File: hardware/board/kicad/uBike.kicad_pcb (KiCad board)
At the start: 2 copper layers, 60 x 80 mm, 56 parts, among them J1 KMDGX-6S-BS, J2 F31S-1A7L1-11040, J3 KMDGX-8S-BS, J4 TC2050-IDC-NL, J5 87520-0010BLF, Q1 MMBT3904, U1 SN65HVD08DR, U2 LD1117S33TR_SOT223, U3 MDBT50Q-P1MV2, U4 PTPSM863252RDXR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

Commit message: Schematic cleanup
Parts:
- C1, C10, C3, C7: value 100nF -> 100n
- C11: value 22pF -> 22p
- C12: value 33uF -> 33u
- C2, C4, C8: value 10uF -> 10u
- C5, C6: value 12pF -> 12p
- C9: value 10nF -> 10n
- moved R15 5.79 mm to (78.0, 46.0), turned to 0 degrees
- moved R14 4.32 mm to (78.0, 40.4), turned to 0 degrees
- moved D1 1.82 mm to (75.5, 43.2), turned to 180 degrees
- moved R13 0.06 mm to (78.8, 43.2)
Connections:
- D1 pad 1: RS485_A -> RS485_B
- D1 pad 2: RS485_B -> RS485_A
- J3 pad 3: Net-(J3-Pad3) -> RS485_B
- J3 pad 4: Net-(J3-Pad4) -> RS485_A
- R13 pad 1: RS485_B -> Net-(U1-B)
- R13 pad 2: RS485_A -> Net-(U1-A)
- R14 pad 1: RS485_B -> RS485_A
- R14 pad 2: Net-(J3-Pad3) -> Net-(U1-A)
- R15 pad 1: RS485_A -> RS485_B
- R15 pad 2: Net-(J3-Pad4) -> Net-(U1-B)
- U1 pad 6: RS485_A -> Net-(U1-A)
- U1 pad 7: RS485_B -> Net-(U1-B)
- U3 pad 3: IN4 -> unconnected-(U3-P1.10-Pad3)
- U3 pad 5: unconnected-(U3-P1.12-Pad5) -> IN4
- U4 pad 10: unconnected-(U4-SW-Pad2) -> (no net)
- U4 pad 11: unconnected-(U4-SW-Pad2) -> (no net)
- U4 pad 12: unconnected-(U4-SW-Pad2) -> (no net)
- U4 pad 13: unconnected-(U4-SW-Pad2) -> (no net)
- U4 pad 14: +5V -> (no net)
- U4 pad 15: +5V -> (no net)
- U4 pad 16: +5V -> (no net)
- U4 pad 17: +5V -> (no net)
- U4 pad 18: +5V -> (no net)
- U4 pad 19: +5V -> (no net)
- U4 pad 8: unconnected-(U4-SW-Pad2) -> (no net)
- U4 pad 9: unconnected-(U4-SW-Pad2) -> (no net)
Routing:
- net Net-(U1-A): track 0.00 -> 23.7 mm
- net Net-(U1-B): track 0.00 -> 23.3 mm
- net RS485_A: track 26.0 -> 10.5 mm, vias 2 -> 1
- net Net-(J3-Pad3): track 14.7 -> 0.00 mm, vias 1 -> 0
- net Net-(J3-Pad4): track 8.51 -> 0.00 mm, vias 1 -> 0
- net RS485_B: track 28.3 -> 22.0 mm, vias 4 -> 1
- net GND: track 0.00 -> 2.77 mm, vias 61 -> 55
- net IN1: track 44.3 -> 42.5 mm
- net IN4: track 37.8 -> 39.4 mm
- net IN3: track 43.0 -> 42.3 mm
- net IN2: track 48.4 -> 47.7 mm

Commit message: Finalized for review
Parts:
- moved R20 8.20 mm to (100.1, 84.5)
- moved D2 6.71 mm to (100.1, 82.0), turned to 0 degrees
- moved J4 4.84 mm to (105.9, 88.0), turned to 90 degrees
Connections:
- U3 pad 36: unconnected-(U3-P0.14-Pad36) -> YU
- U3 pad 57: YU -> unconnected-(U3-P1.06-Pad57)
- U4 pad 10: (no net) -> unconnected-(U4-SW-Pad2)
- U4 pad 11: (no net) -> unconnected-(U4-SW-Pad2)
- U4 pad 12: (no net) -> unconnected-(U4-SW-Pad2)
- U4 pad 13: (no net) -> unconnected-(U4-SW-Pad2)
- U4 pad 14: (no net) -> +5V
- U4 pad 15: (no net) -> +5V
- U4 pad 16: (no net) -> +5V
- U4 pad 17: (no net) -> +5V
- U4 pad 18: (no net) -> +5V
- U4 pad 19: (no net) -> +5V
- U4 pad 8: (no net) -> unconnected-(U4-SW-Pad2)
- U4 pad 9: (no net) -> unconnected-(U4-SW-Pad2)
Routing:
- net GND: track 2.77 -> 26.7 mm, vias 55 -> 69
- net +3.3V: track 132.7 -> 144.2 mm
- net Net-(D2-A): track 17.4 -> 7.79 mm, vias 2 -> 0
- net SWD_RST: track 10.4 -> 19.0 mm
- net SWO: track 10.5 -> 17.6 mm
- net YU: track 46.1 -> 42.0 mm
- net BL_PWM: track 22.2 -> 24.5 mm
- net SWCLK: track 13.9 -> 11.9 mm, vias 2 -> 0
- net CTP_SDA: track 42.7 -> 43.4 mm
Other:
- board text removed: "Greco Engineering Solutions LLC"

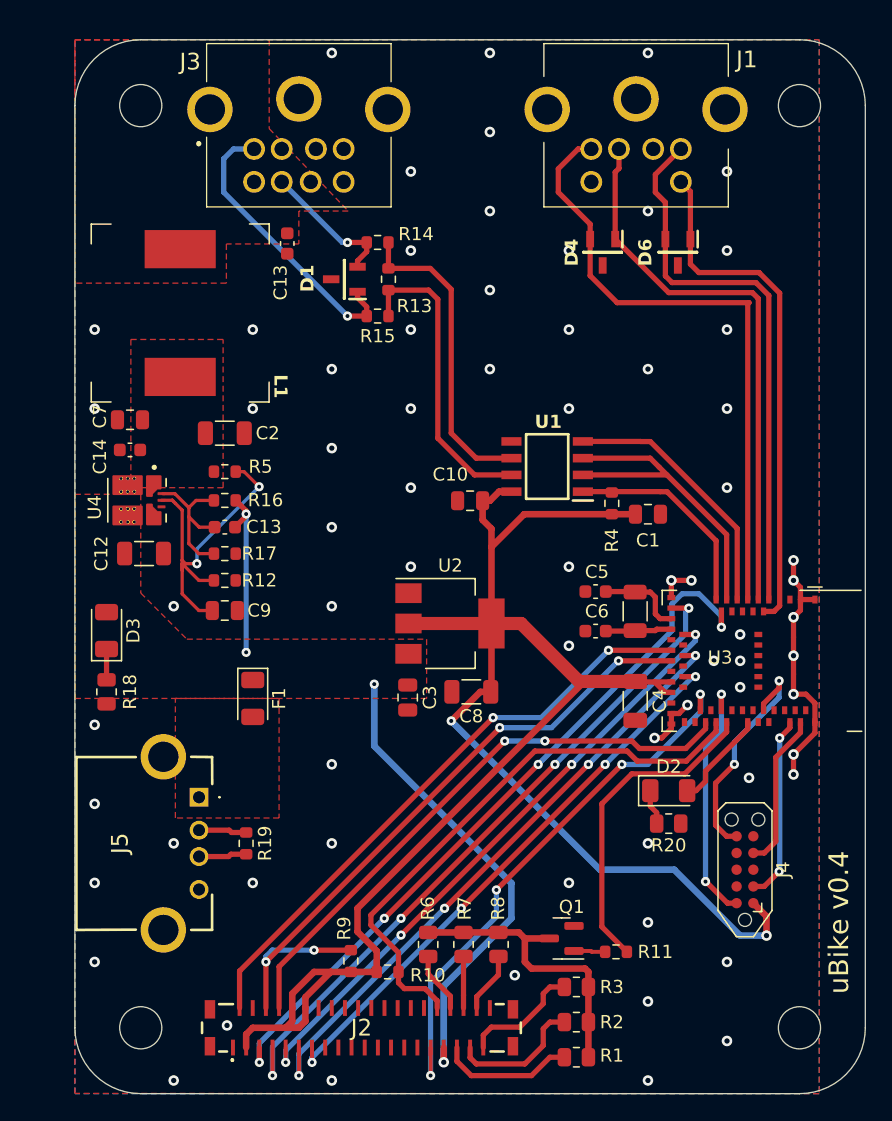
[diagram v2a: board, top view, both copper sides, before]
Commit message: Changed 2.2uF cap footprints and a bit more cleanup
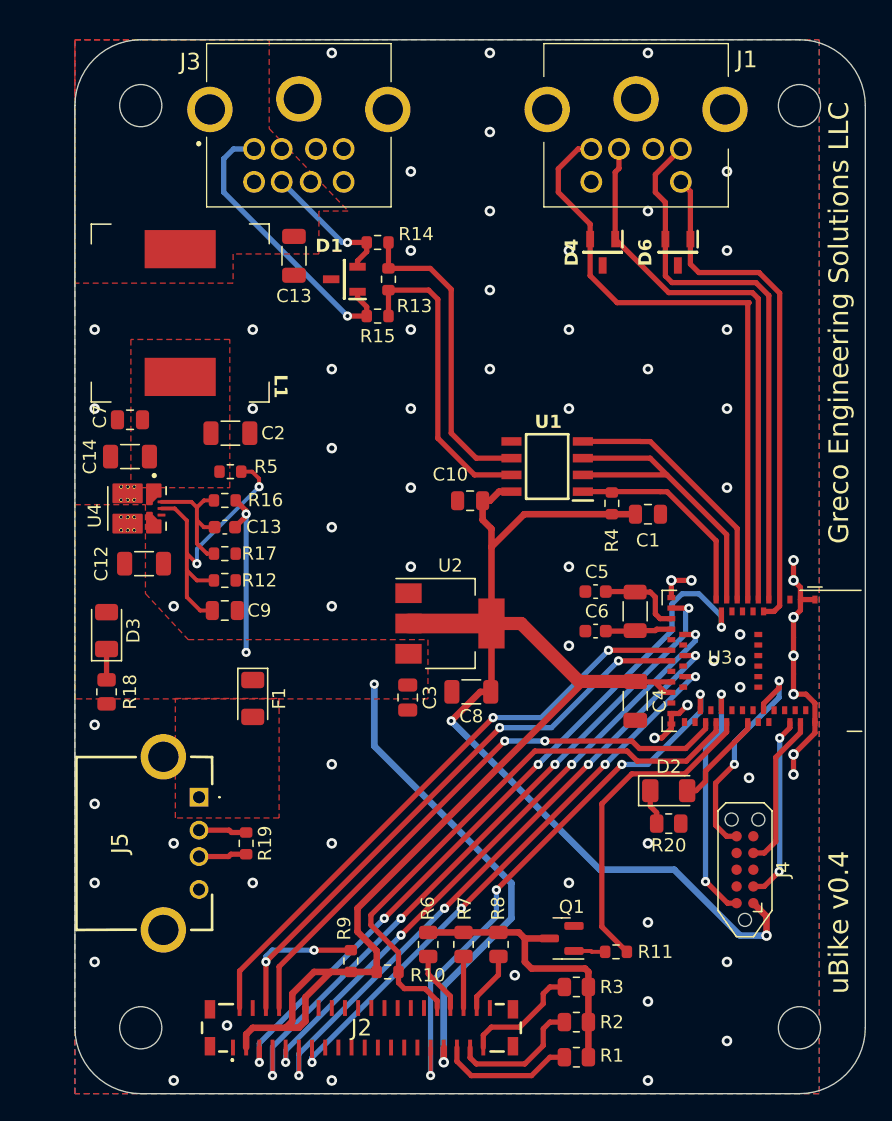
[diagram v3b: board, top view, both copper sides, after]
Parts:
- C13, C14: footprint Capacitor_SMD:C_0603_1608Metric -> Capacitor_SMD:C_1206_3216Metric
- L1: value 120 -> 120u
- moved C13 1.06 mm to (71.6, 41.4)
- moved C12 0.77 mm to (60.2, 64.8)
- moved U4 0.62 mm to (59.7, 60.6)
- moved C14 0.51 mm to (59.2, 56.6)
- moved C2 0.42 mm to (66.8, 54.9)
- moved R5 0.42 mm to (66.8, 57.8)
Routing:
- net Net-(U4-EN): track 25.9 -> 23.9 mm
- net Net-(U4-FB): track 11.8 -> 10.3 mm
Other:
- board text added: "Greco Engineering Solutions LLC"

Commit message: Added inline resistors for ESD on inputs, created order T-V26W325984A
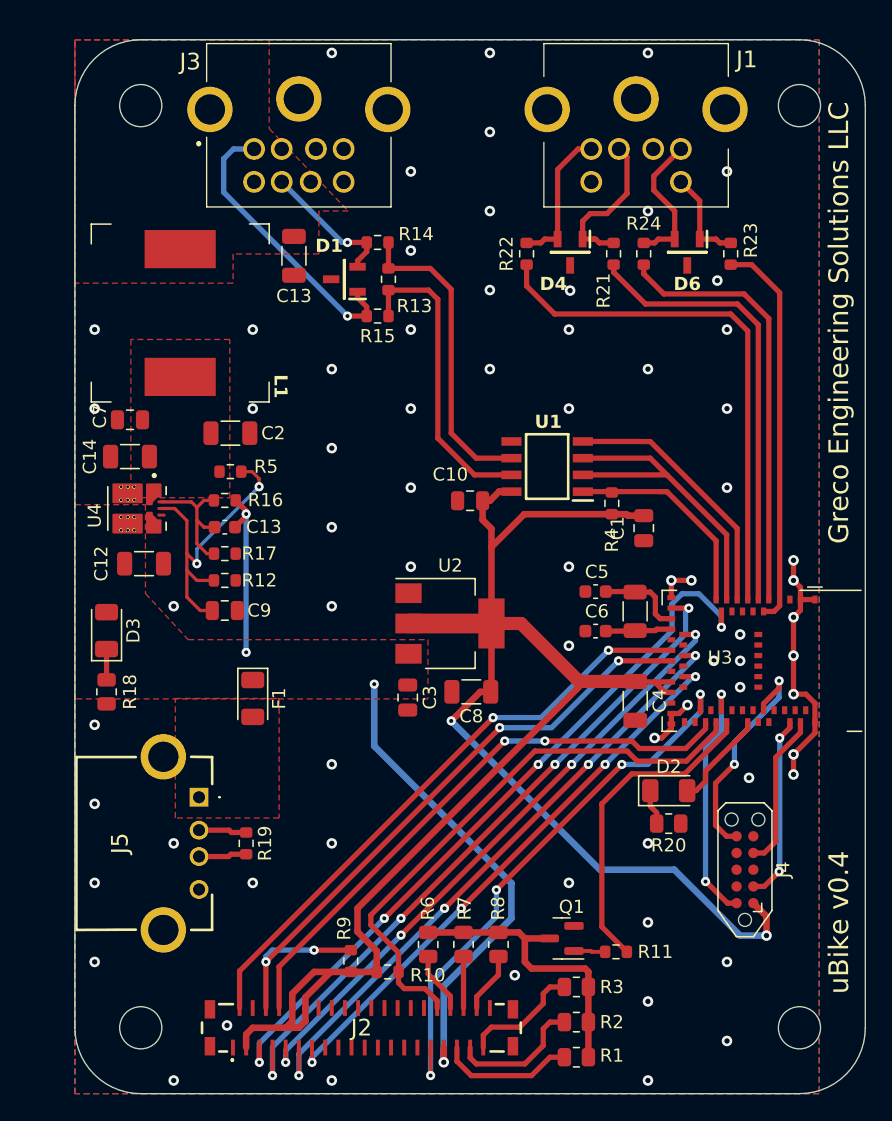
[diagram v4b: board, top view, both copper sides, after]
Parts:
- added R21: 10, Resistor_SMD:R_0603_1608Metric, F.Cu at (95.9, 41.2)
- added R22: 10, Resistor_SMD:R_0603_1608Metric, F.Cu at (89.3, 41.2)
- added R23: 10, Resistor_SMD:R_0603_1608Metric, F.Cu at (104.8, 41.2)
- added R24: 10, Resistor_SMD:R_0603_1608Metric, F.Cu at (98.2, 41.2)
- R10, R9: value 1k7 -> 1k69
- R19: value 157 -> 150
- moved D4 2.47 mm to (92.6, 41.1)
- moved C1 1.11 mm to (98.2, 62.1), turned to -90 degrees
- moved D6 0.71 mm to (101.5, 41.1)
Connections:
- D4 pad 1: IN1 -> Net-(D4-Pad1)
- D4 pad 2: IN2 -> Net-(D4-Pad2)
- D6 pad 1: IN4 -> Net-(D6-Pad1)
- D6 pad 2: IN3 -> Net-(D6-Pad2)
- J1 pad 1: IN1 -> Net-(D4-Pad1)
- J1 pad 3: IN2 -> Net-(D4-Pad2)
- J1 pad 5: IN3 -> Net-(D6-Pad2)
- J1 pad 8: IN4 -> Net-(D6-Pad1)
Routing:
- net Net-(D4-Pad1): track 0.00 -> 11.7 mm
- net Net-(D4-Pad2): track 0.00 -> 11.0 mm
- net Net-(D6-Pad2): track 0.00 -> 10.8 mm
- net IN4: track 39.4 -> 29.8 mm
- net IN3: track 42.3 -> 32.9 mm
- net IN1: track 42.5 -> 34.1 mm
- net IN2: track 47.7 -> 40.2 mm
- net Net-(D6-Pad1): track 0.00 -> 7.41 mm
- net +3.3V: track 144.0 -> 144.7 mm
